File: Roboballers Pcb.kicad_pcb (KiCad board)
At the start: 2 copper layers, 120 x 120 mm, 114 parts, among them J1 Conn_01x02, J2 Conn_01x02, J3 Conn_01x02, J4 Conn_01x02, J5 Screw_Terminal_01x02, J6 Conn_01x02, J7 Bottom_Pcb, SW1 OS102011MS2QN1, SW2 OS102011MS2QN1, SW3 OS102011MS2QN1, SW4 OS102011MS2QN1, U1 VNH7070ASTR, U10 TSOP25xx, U11 OpenMV_H7_R2, U12 MCP3008, U13 TSOP25xx, U14 TSOP25xx, U15 SEN0140, U16 TSOP25xx, U17 RockerSwitch, U18 TSOP25xx, U19 TSOP25xx, U2 VNH7070ASTR, U20 TSOP25xx, U21 TSOP25xx, U22 TSOP25xx, U23 TSOP25xx, U24 TSOP25xx, U25 TSOP25xx, U26 TSOP25xx, U27 MCP3008, U28 MCP3008, U29 TSOP25xx, U3 VNH7070ASTR, U30 TSOP25xx, U31 TSOP25xx, U32 TSOP25xx, U33 TSOP25xx, U34 TSOP25xx, U35 TSOP25xx, U36 TSOP25xx, U4 VNH7070ASTR, U5 Teensy4.1, U6 TSOP25xx, U7 V_Regulator_-_5v, U8 TSOP25xx, U9 TSOP25xx

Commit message: good stuff
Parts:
- moved U15 97.8 mm to (175.7, 51.5)
- moved U11 14.0 mm to (100.0, 100.0)
- moved U4 10.6 mm to (125.5, 64.6)
- moved U5 10.0 mm to (100.2, 69.6), turned to 180 degrees
- moved U28 6.08 mm to (69.1, 97.0)
- moved J4 5.77 mm to (117.4, 64.8)
- moved U12 0.41 mm to (122.2, 114.6)
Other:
- outline, holes or cut-outs redrawn

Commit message: nice
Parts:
- added D1: LED, LED_THT:LED_D1.8mm_W1.8mm_H2.4mm_Horizontal_O1.27mm_Z1.6mm, F.Cu at (109.8, 89.6)
- added R40: R_Photo, OptoDevice:R_LDR_4.9x4.2mm_P2.54mm_Vertical, F.Cu at (105.2, 89.4)
- U15, U4: moved to F.Cu
- moved C3 216.5 mm to (65.6, 129.3), turned to 180 degrees
- moved C2 190.9 mm to (87.1, 61.7), turned to -90 degrees
- moved R3 189.0 mm to (64.5, 82.0)
- moved R30 173.6 mm to (94.2, 87.1), turned to 180 degrees
- moved R4 168.2 mm to (85.3, 87.0), turned to 180 degrees
- moved R11 168.2 mm to (90.2, 87.1)
- moved C4 165.2 mm to (111.9, 80.5)
- moved R12 147.1 mm to (112.0, 71.6)
- moved R6 146.5 mm to (111.3, 128.0)
- moved R5 146.3 mm to (111.3, 124.2), turned to 180 degrees
- moved R28 138.4 mm to (130.8, 67.5), turned to 90 degrees
- moved R8 128.1 mm to (126.0, 87.6), turned to 180 degrees
- moved R16 127.8 mm to (134.6, 131.3)
- moved R7 127.6 mm to (126.0, 91.2), turned to 180 degrees
- moved U15 117.9 mm to (66.0, 94.7), turned to 0 degrees
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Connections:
- U5 pad 12: unconnected-(U5-10_CS_MQSR-Pad12) -> R_Photo
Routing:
- net GND: track 0.00 -> 841.9 mm, vias 0 -> 7
- net 3.3v: track 0.00 -> 555.3 mm, vias 0 -> 4
- net 12v: track 0.00 -> 197.7 mm, vias 0 -> 6
- net MISO: track 0.00 -> 175.5 mm, vias 0 -> 2
- net MOSI: track 0.00 -> 173.8 mm, vias 0 -> 1
- net SCK(Clock Timing): track 0.00 -> 172.3 mm, vias 0 -> 2
- net 5v: track 0.00 -> 135.6 mm, vias 0 -> 2
- net Net-(U27-CH0): track 0.00 -> 100.3 mm, vias 0 -> 3
- net Calibrate : track 0.00 -> 96.5 mm, vias 0 -> 1
- net Direction2(1): track 0.00 -> 92.9 mm, vias 0 -> 2
- net Offense: track 0.00 -> 92.0 mm, vias 0 -> 1
- net CHIPSELECTIR2: track 0.00 -> 87.3 mm, vias 0 -> 2
- net Blue: track 0.00 -> 79.8 mm, vias 0 -> 1
- net Direction1(1): track 0.00 -> 76.1 mm, vias 0 -> 2
- net CHIPSELECTIR1: track 0.00 -> 75.3 mm
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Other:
- outline, holes or cut-outs redrawn
- copper layers 2 -> 4

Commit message: nice stuff fixed all stuff
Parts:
- removed U6: TSOP25xx, ir sensor:TO_SP4038_VIS
- moved U2 0.31 mm to (80.6, 75.8)
- turned U3 to 180 degrees
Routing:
- net 12v: track 197.7 -> 319.0 mm, vias 6 -> 36
- net Net-(J4-Pin_1): track 30.8 -> 123.2 mm, vias 1 -> 7
- net 3.3v: track 555.3 -> 641.6 mm, vias 4 -> 0
- net Net-(J2-Pin_2): track 24.1 -> 70.7 mm, vias 0 -> 7
- net GND: track 841.9 -> 810.0 mm, vias 7 -> 4
- net Net-(J2-Pin_1): track 25.5 -> 56.1 mm, vias 1 -> 6
- net Net-(U12-CH7): track 67.8 -> 93.5 mm, vias 2 -> 0
- net Net-(J3-Pin_1): track 42.7 -> 66.8 mm, vias 0 -> 6
- net Net-(J1-Pin_1): track 28.5 -> 50.3 mm, vias 2 -> 6
- net MISO: track 175.5 -> 159.6 mm, vias 2 -> 3
- net Net-(U4-INA): track 16.1 -> 31.1 mm
- net Net-(J4-Pin_2): track 33.2 -> 48.2 mm, vias 1 -> 7
- net Net-(U27-CH1): track 68.1 -> 80.5 mm, vias 1 -> 2
- net Net-(J3-Pin_2): track 40.5 -> 50.8 mm, vias 0 -> 6
- net Net-(U4-INB): track 11.0 -> 20.7 mm, vias 0 -> 2
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
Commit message: I AM HIMMMMM
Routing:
- net 3.3v: track 641.6 -> 574.0 mm
- net Net-(U12-CH7): track 93.5 -> 58.6 mm, vias 0 -> 2
- net Offense: track 87.7 -> 116.7 mm
- net GND: track 810.0 -> 793.5 mm, vias 4 -> 6
- net Net-(U27-CH1): track 80.5 -> 66.4 mm, vias 2 -> 1
- net SCK(Clock Timing): track 169.5 -> 181.3 mm
- net CHIPSELECTIR1: track 80.7 -> 90.9 mm
- net Net-(U2-PWM): track 20.3 -> 30.1 mm
- net Net-(U27-CH0): track 92.8 -> 84.8 mm, vias 2 -> 3
- net Blue: track 83.4 -> 75.4 mm, vias 1 -> 2
- net Net-(U28-CH3): track 41.3 -> 34.6 mm
- net Net-(J2-Pin_2): track 70.7 -> 76.0 mm, vias 7 -> 10
- net Calibrate : track 91.8 -> 96.8 mm, vias 2 -> 1
- net Net-(U4-INB): track 20.7 -> 16.2 mm
- net Net-(U2-INB): track 9.20 -> 13.6 mm
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- added copper zone on B.Cu, net GND
- added copper zone on F.Cu, net GND
- added copper zone on In1.Cu, net GND
- added copper zone on In2.Cu, net GND

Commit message: i am him part 2
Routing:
- net 3.3v: track 574.0 -> 582.6 mm
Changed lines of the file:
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@@
 	)
 	(segment
-		(start 54.6787 129.203)
-		(end 63.608 138.132)
+		(start 54.4997 129.203)
+		(end 54.4997 137.549598)
 		(width 1)
 		(layer "In1.Cu")
@@
 	)
 	(segment
+		(start 54.750101 137.856869)
+		(end 55.742914 139.012929)
+		(width 1)
+		(layer "In1.Cu")
+		(net 35)
+	)
+	(segment
 		(start 88.4757 151.961)
 		(end 88.4757 152.392)
@@
 	)
 	(segment
+		(start 55.742914 139.012929)
+		(end 55.783425 139.058)
+		(width 1)
+		(layer "In1.Cu")
+		(net 35)
+	)
+	(segment
 		(start 56.911 106.416)
 		(end 56.911 108.012)
@@
 	)
 	(segment
-		(start 63.608 138.132)
-		(end 63.608 139.058)
+		(start 55.783425 138.772416)
+		(end 59.725955 134.829886)
 		(width 1)
 		(layer "In1.Cu")
@@
 	)
 	(segment
+		(start 59.725955 134.829886)
+		(end 60.305855 134.829886)
+		(width 1)
+		(layer "In1.Cu")
+		(net 35)
+	)
+	(segment
 		(start 116.431 151.508)
 		(end 124.117 151.508)
@@
 	)
 	(segment
+		(start 54.4997 137.549598)
+		(end 54.750101 137.856869)
+		(width 1)
+		(layer "In1.Cu")
+		(net 35)
+	)
+	(segment
 		(start 133.724 90.17)
 		(end 132.816 89.262)
@@
 	)
 	(segment
+		(start 55.783425 139.058)
+		(end 55.783425 138.772416)
+		(width 1)
+		(layer "In1.Cu")
+		(net 35)
+	)
+	(segment
 		(start 68.0626 139.984)
 		(end 70.4652 142.387)
@@
 	)
 	(segment
+		(start 63.608 138.132031)
+		(end 63.608 139.058)
+		(width 1)
+		(layer "In1.Cu")
+		(net 35)
+	)
+	(segment
 		(start 73.4452 142.387)
 		(end 78.672 137.16)
@@
 	)
 	(segment
+		(start 60.305855 134.829886)
+		(end 63.608 138.132031)
+		(width 1)
+		(layer "In1.Cu")
+		(net 35)
+	)
+	(segment
 		(start 139.984 136.392)
 		(end 139.9841 136.392)
@@
 		(layer "In1.Cu")
 		(net 35)
-	)
-	(segment
-		(start 54.4997 129.203)
-		(end 54.6787 129.203)
-		(width 1)
-		(layer "In1.Cu")
-		(net 35)

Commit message: should be done now!!
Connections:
- J6 pad 1: Net-(J5-Pin_2) -> 12v
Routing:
- net Net-(J5-Pin_2): track 35.3 -> 10.4 mm
- net 12v: track 318.6 -> 323.6 mm
- net Net-(U16-OUT): track 9.28 -> 6.96 mm
- net MISO: track 161.9 -> 160.2 mm

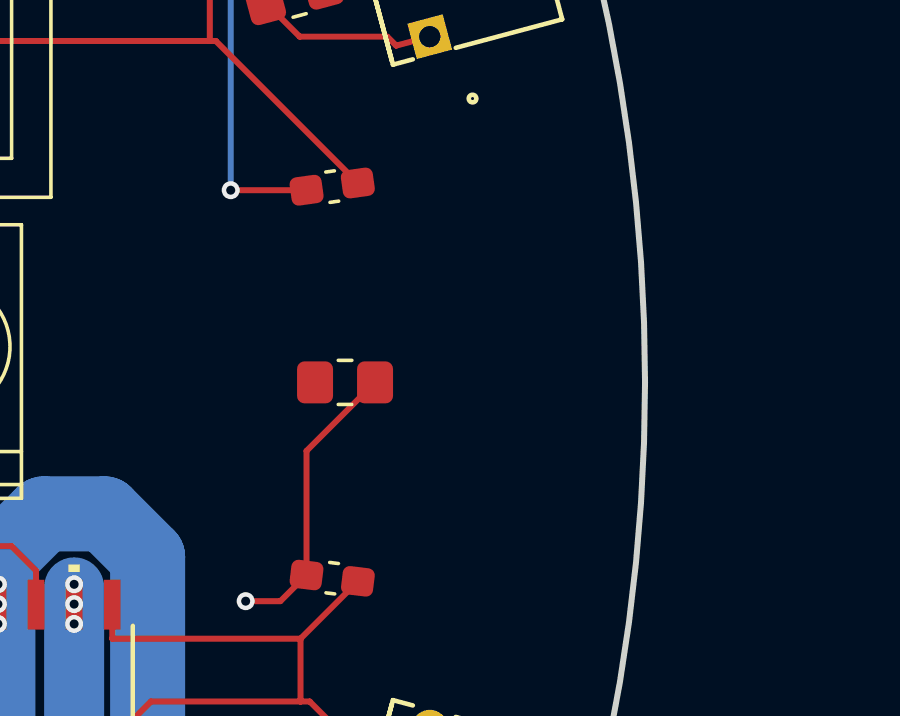
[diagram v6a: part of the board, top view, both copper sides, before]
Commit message: oh no 1 line sensor got cooked
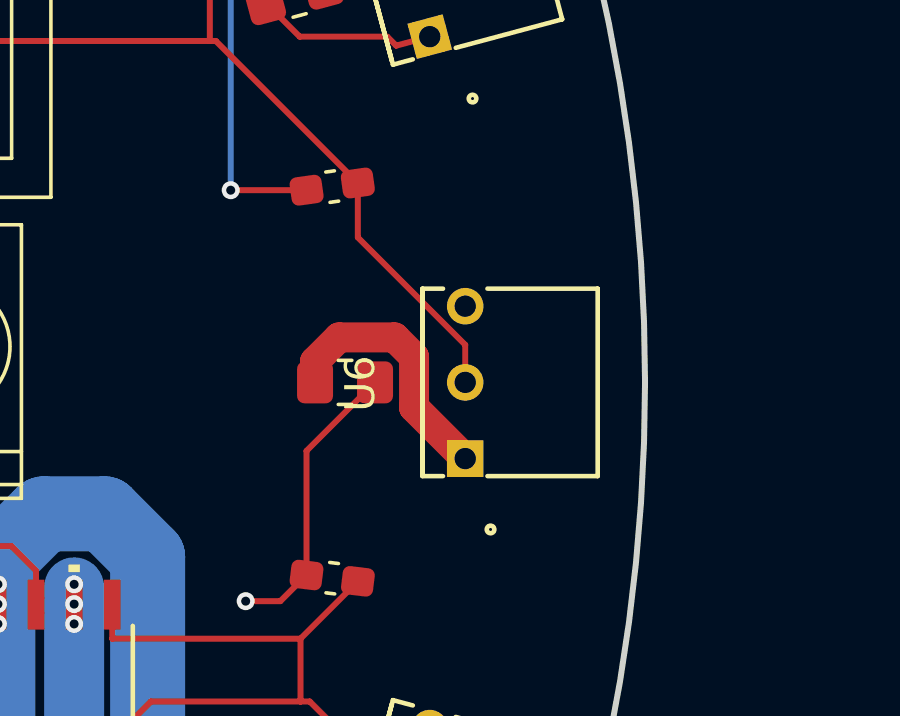
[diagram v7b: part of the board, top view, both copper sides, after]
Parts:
- added U6: TSOP25xx, ir sensor:TO_SP4038_VIS, F.Cu at (154.0, 100.0)
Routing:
- net Net-(U6-OUT): track 0.00 -> 8.70 mm
- net GND: track 793.5 -> 801.7 mm
- net 3.3v: track 582.6 -> 586.2 mm
